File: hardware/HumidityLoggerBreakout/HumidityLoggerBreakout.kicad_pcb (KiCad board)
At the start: 2 copper layers, 98 x 74 mm, 45 parts, among them J1 PWR_IN, J2 BME280, J3 +5V_OUT, J4 IO, J6 Conn_01x11, J7 Conn_01x11, J8 I2C_MCU, U1 LM317_TO-252

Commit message: WIP on the board.
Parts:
- removed the C2 at (104.0, 65.7)
- removed C3, C4, C6, C7, C8: 100n, Capacitor_SMD:C_0805_2012Metric_Pad1.18x1.45mm_HandSolder
- removed C5: 100u, Capacitor_Tantalum_SMD:CP_EIA-3528-12_Kemet-T_Pad1.50x2.35mm_HandSolder
- removed the D3 at (97.0, 87.0)
- removed the J1 at (88.0, 69.0)
- removed the J3 at (86.0, 80.5)
- removed R11: 330, Resistor_SMD:R_0805_2012Metric_Pad1.20x1.40mm_HandSolder
- removed R13, R9: 1k, Resistor_SMD:R_0805_2012Metric_Pad1.20x1.40mm_HandSolder
- removed REF** (x6): VLP-XXX-X, marcin_library:VLP-XXX-X
- removed U1: LM317_TO-252, Package_TO_SOT_SMD:TO-252-2
- J2: renamed from J6; footprint Connector_PinHeader_2.54mm:PinHeader_1x11_P2.54mm_Vertical -> Connector_PinSocket_2.54mm:PinSocket_1x11_P2.54mm_Vertical
- J3: renamed from J8; footprint Connector_PinHeader_2.54mm:PinHeader_1x04_P2.54mm_Vertical -> Connector_PinSocket_2.54mm:PinSocket_1x04_P2.54mm_Vertical
- J5: renamed from J7; footprint Connector_PinHeader_2.54mm:PinHeader_1x11_P2.54mm_Vertical -> Connector_PinSocket_2.54mm:PinSocket_1x11_P2.54mm_Vertical
- moved C1 19.3 mm to (120.8, 58.3), turned to -90 degrees
- moved H1 17.5 mm to (94.0, 46.0)
- moved H4 16.0 mm to (94.0, 107.0)
- moved D7 14.3 mm to (131.8, 107.2)
- moved D6 14.3 mm to (126.9, 107.2)
- moved R6 14.3 mm to (140.7, 107.7)
- moved R7 14.3 mm to (140.6, 105.5)
- moved D1 11.9 mm to (100.5, 107.2)
- moved D2 11.9 mm to (105.3, 107.2)
- moved D3 11.9 mm to (110.2, 107.2)
- moved D4 11.9 mm to (115.0, 107.2)
- moved H2 9.90 mm to (161.0, 46.0)
- moved H3 7.00 mm to (161.0, 107.0)
- renumbered C9 to C2, D6 to D1, D7 to D2, D8 to D3, D9 to D4, D1 to D5, D2 to D6, D5 to D7, J4 to J1, J2 to J4, R5 to R1, R6 to R2, R7 to R3, R8 to R4, R10 to R5, R12 to R6, R15 to R7
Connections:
- C1 pad 1: +12V -> +3.3V
- J1 pad 1: +5V -> +3.3V
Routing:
- net +5V: track 69.8 -> 0.00 mm, vias 55 -> 0
- net +12V: track 32.2 -> 0.00 mm
- net /A3: track 21.9 -> 7.95 mm
- net +3.3V: track 84.7 -> 98.4 mm
- net /D3: track 74.7 -> 87.4 mm
- net Net-(D4-Pad2): track 6.25 -> 15.4 mm
- net Net-(R11-Pad2): track 7.97 -> 0.00 mm
- net Net-(D3-Pad2): track 6.35 -> 13.0 mm
- net Net-(D2-Pad2): track 7.31 -> 10.9 mm
- net Net-(D3-Pad2) (its old number): track 1.97 -> 0.00 mm
- net Net-(D7-Pad1): track 9.73 -> 8.99 mm
- net GND: track 20.8 -> 20.6 mm, vias 20 -> 19
- removed copper zone on B.Cu, net +5V
- removed copper zone on F.Cu, net +5V
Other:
- board size 98 x 74 mm -> 75 x 81 mm
- board text removed: "+5V"
- board text removed: "-"

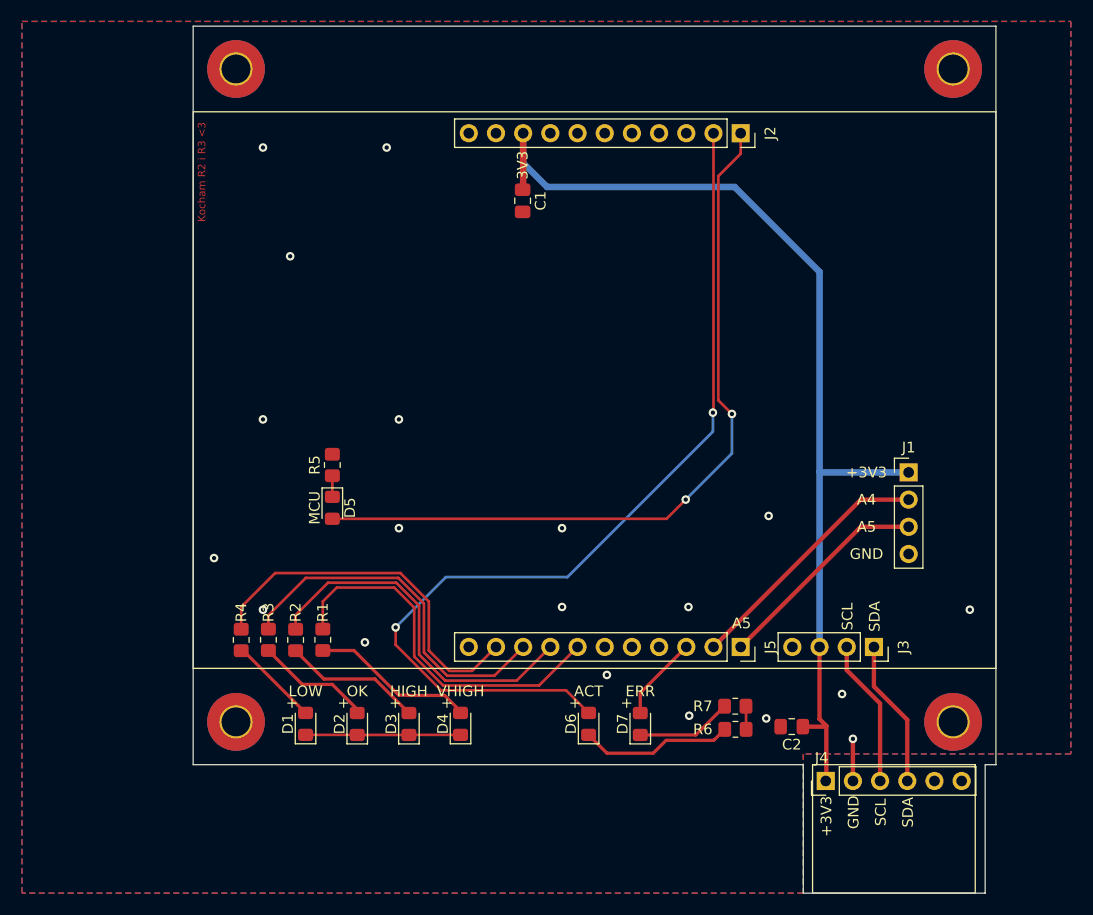
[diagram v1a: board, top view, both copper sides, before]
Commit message: After updating the firmware USERDATA can be used again.
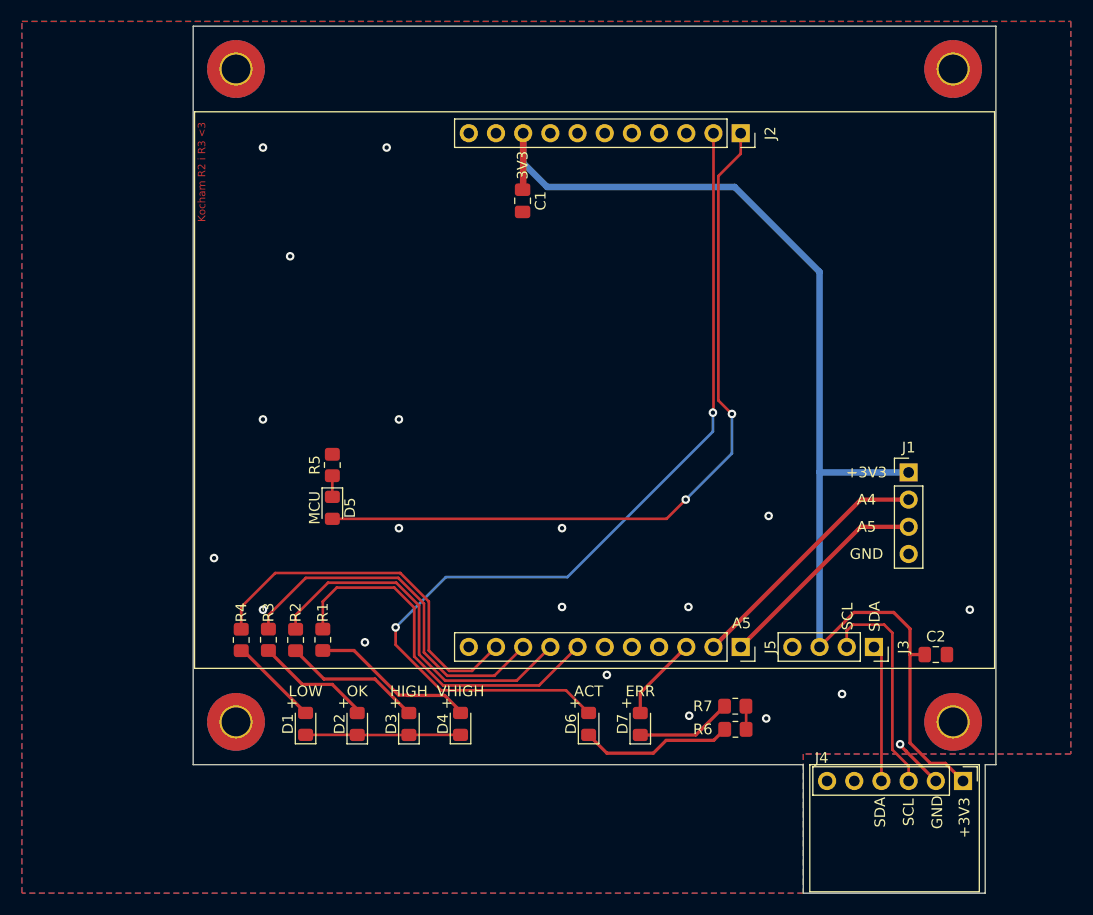
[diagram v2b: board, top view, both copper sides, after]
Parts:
- moved C2 15.1 mm to (159.4, 100.7), turned to 0 degrees
- moved J4 12.8 mm to (161.9, 112.5), turned to -90 degrees
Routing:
- net +3.3V: track 98.4 -> 112.3 mm
- net /SCL: track 13.8 -> 20.8 mm
- net /SDA: track 13.8 -> 12.8 mm
- net GND: track 20.6 -> 21.5 mm
